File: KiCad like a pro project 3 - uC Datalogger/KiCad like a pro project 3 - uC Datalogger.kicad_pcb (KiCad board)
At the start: 2 copper layers, 53.8 x 34 mm, 29 parts, among them J1 Conn_01x04_Male, J2 Conn_01x09_Male, J3 Conn_01x04_Male, J4 Conn_02x03_Odd_Even, U1 24LC1025, U2 24LC1025, U3 DS1337S+, U4 ATMEGA328P_VQFNVQFN, Y1 32.768 KHz, Y2 16 MHz

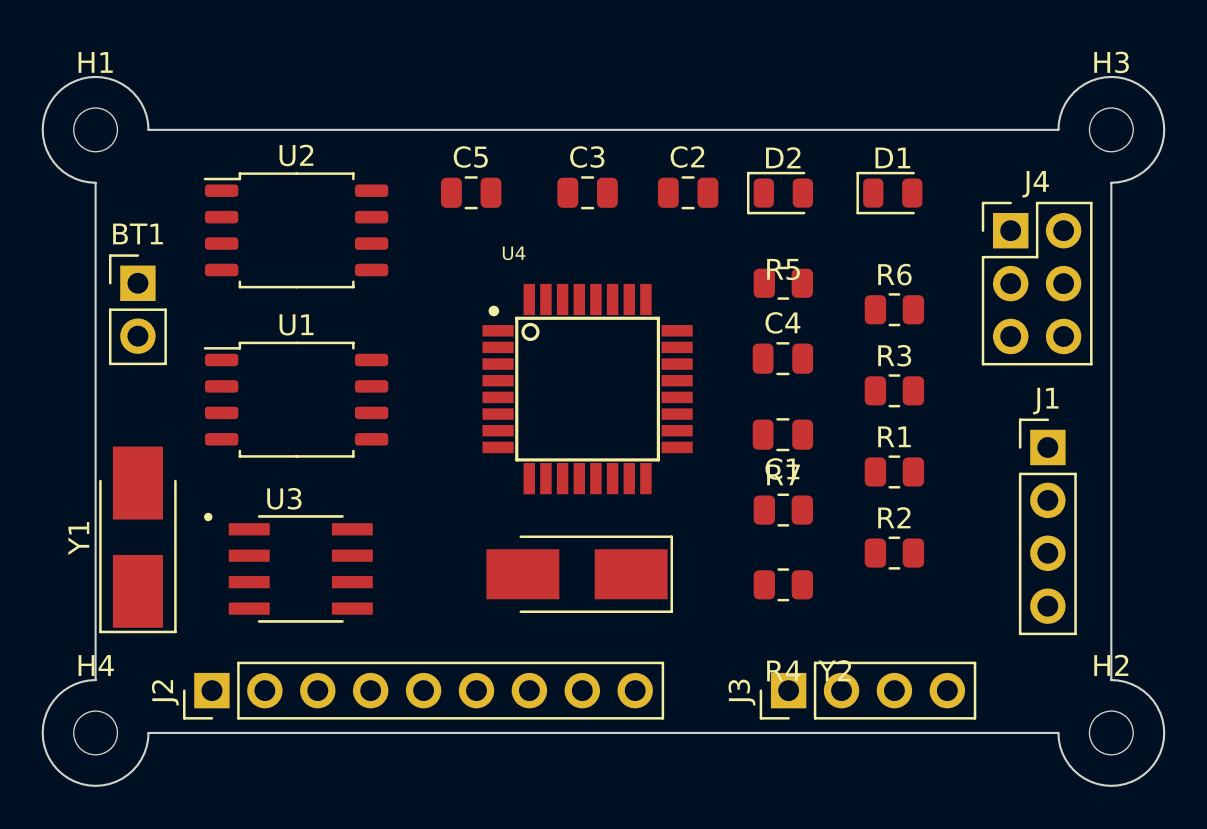
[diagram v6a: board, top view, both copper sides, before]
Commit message: added front and back silkscreen
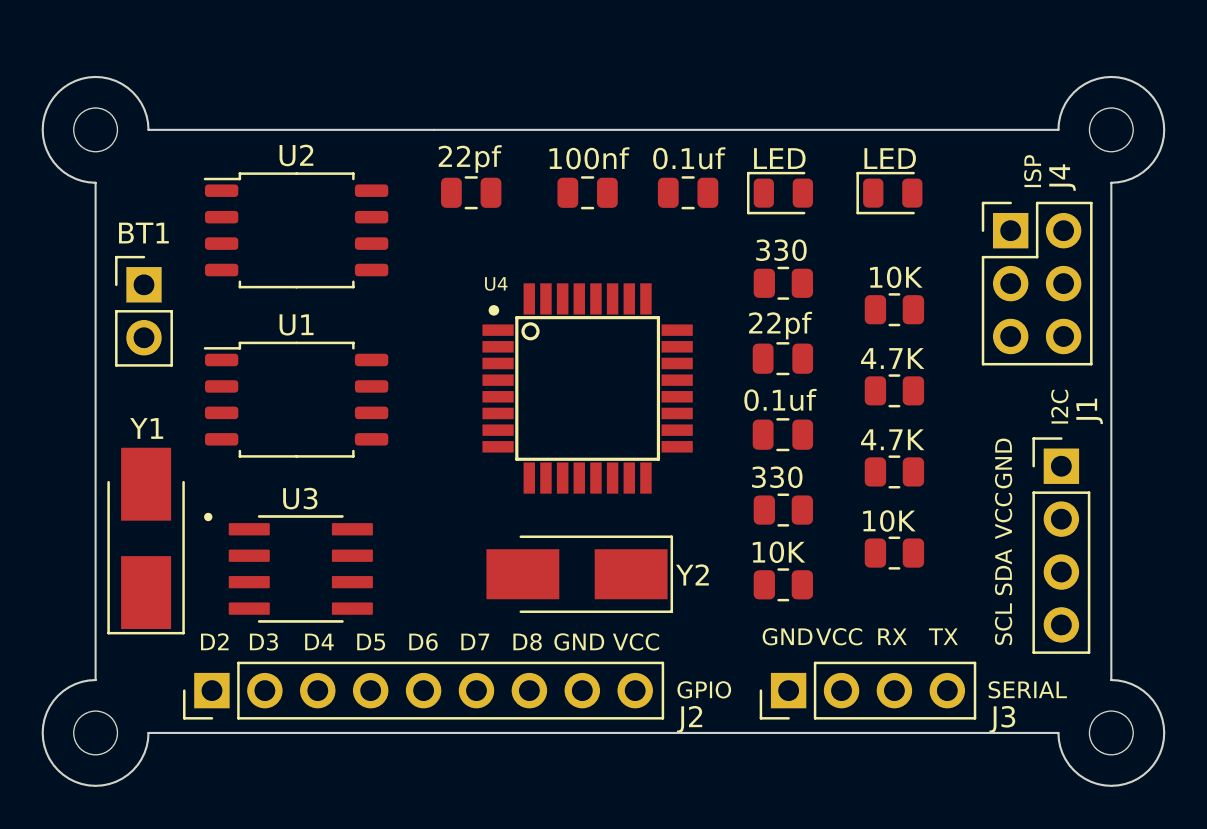
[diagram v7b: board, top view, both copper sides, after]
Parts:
- added REF**: KiCad-Logo2_5mm_SilkScreen, Symbol:KiCad-Logo2_5mm_SilkScreen, B.Cu at (59.1, 91.0)
- moved J1 1.11 mm to (95.6, 104.0)
- moved Y1 0.40 mm to (51.7, 107.5)
- moved BT1 0.30 mm to (51.6, 95.3)
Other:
- board text added: "D2"
- board text added: "D3"
- board text added: "D4"
- board text added: "D5"
- board text added: "D6"
- board text added: "D7"
- board text added: "D8"
- board text added: "GND"
- board text added: "GPIO"
- board text added: "I2C"
- board text added: "ISP"
- board text added: "MCU Datalogger with EEPROM Designed by: Casper R. Tak"
- board text added: "RX"
- board text added: "SCL"
- board text added: "SDA"
- board text added: "SERIAL"
- board text added: "TX"
- board text added: "V0.1"
- board text added: "VCC"

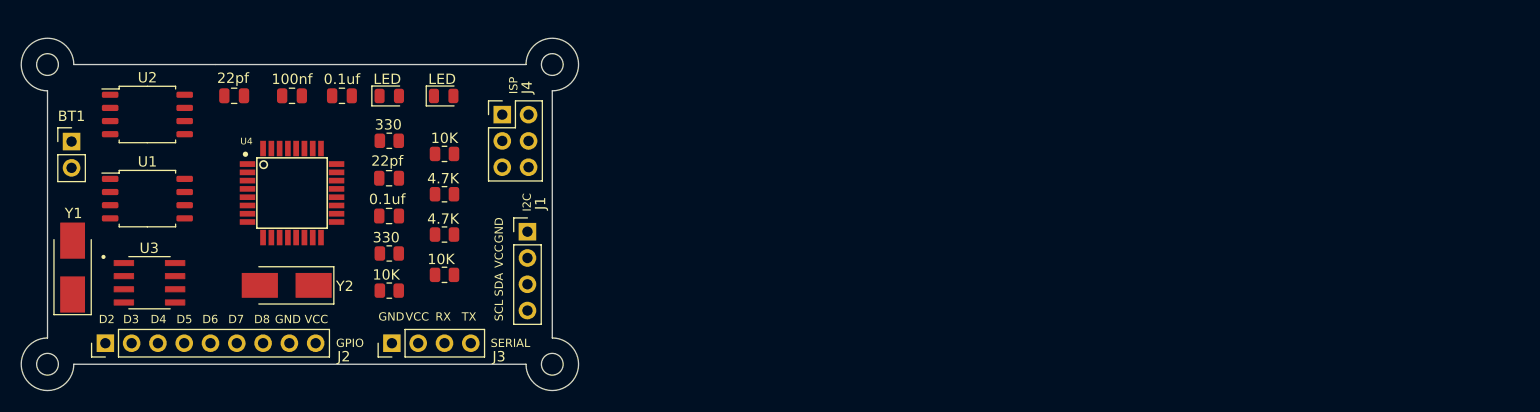
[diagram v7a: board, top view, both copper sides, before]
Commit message: repositioned pcb to center of workfield
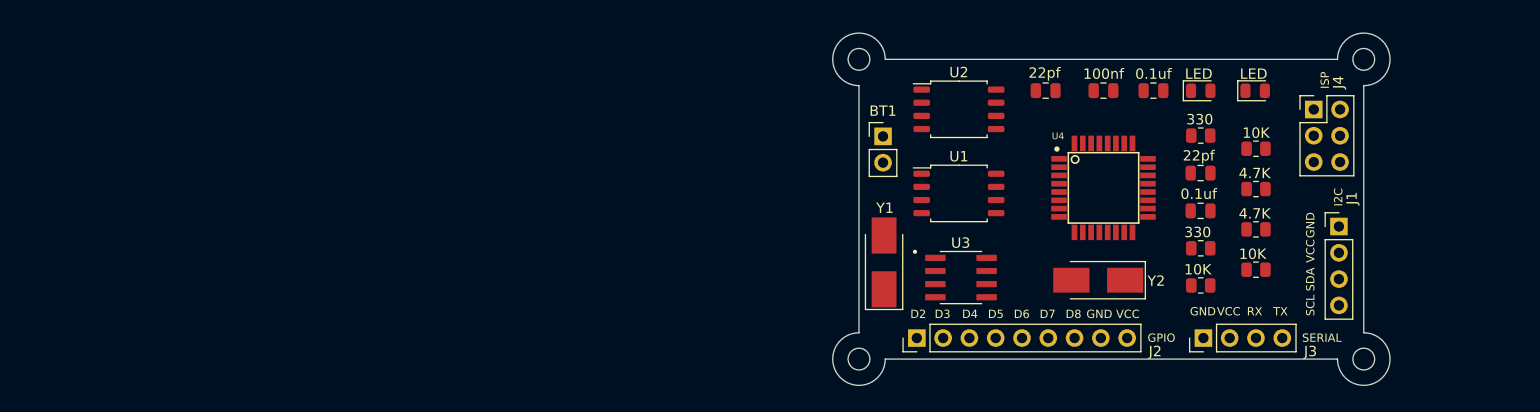
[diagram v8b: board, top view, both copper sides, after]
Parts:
- moved BT1 78.4 mm to (130.0, 94.8)
- moved C3 78.4 mm to (151.3, 90.4)
- moved C5 78.4 mm to (145.7, 90.4)
- moved D1 78.4 mm to (166.0, 90.4)
- moved H1 78.4 mm to (127.7, 87.4)
- moved H4 78.4 mm to (127.7, 116.3)
- moved J2 78.4 mm to (133.3, 114.3)
- moved J4 78.4 mm to (171.6, 92.2)
- moved R1 78.4 mm to (166.0, 103.8)
- moved R2 78.4 mm to (166.0, 107.7)
- moved R3 78.4 mm to (166.0, 99.9)
- moved R6 78.4 mm to (166.0, 96.0)
- moved REF** 78.4 mm to (137.5, 90.5)
- moved U1 78.4 mm to (137.3, 100.3)
- moved U2 78.4 mm to (137.3, 92.2)
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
